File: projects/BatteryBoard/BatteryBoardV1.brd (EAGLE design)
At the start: 99 x 99 mm, 157 parts, among them M1 BSO201SP, U1 LTC4412MPS6, U2 SM74611, U3 LTC4121, U4 LTC4121, U5 LTC4121, U6 LTC4121

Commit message: Nearly finished placement of battery board, continued library updates and touch ups on all active boards/schematics.
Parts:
- removed U$4, U$6: BTS555, BrownSpaceEngineering:TO218-5
- removed U2: SM74611, BrownSpaceEngineering:TO-263
- added C23, C24, C26, C27: 10nF, BrownSpaceEngineering:0805
- added C25, C28: 150nF, BrownSpaceEngineering:0805
- added D7: DFLS130L, BrownSpaceEngineering:PWRDI-123
- added LIFE1TEMP, LIFE3TEMP, LION1TEMP, LION2TEMP: (no value), BrownSpaceEngineering:FLATPACK
- added R77, R80: 1K, BrownSpaceEngineering:0805
- added R78, R79, R81, R82: 4.7K, BrownSpaceEngineering:0805
- added R83: (no value), BrownSpaceEngineering:0805
- added SW1, SW2: BTS50015-1TAD, BrownSpaceEngineering:TO-263-7-8
- added V31: LIFEB1_OUTSNS, BrownSpaceEngineering:VIA-60MIL
- added V32: LION2SNS, BrownSpaceEngineering:VIA-60MIL
- added V33: LION2_RUN_CHG, BrownSpaceEngineering:VIA-60MIL
- added V34: LION1_RUN_DISG, BrownSpaceEngineering:VIA-60MIL
- added V35: LION2_RUN_DISG, BrownSpaceEngineering:VIA-60MIL
- added V36: LION1_STAT, BrownSpaceEngineering:VIA-60MIL
- added V37: LIONREF, BrownSpaceEngineering:VIA-60MIL
- added V38: LION2_STAT, BrownSpaceEngineering:VIA-60MIL
- added V39: UMB_CHG, BrownSpaceEngineering:VIA-60MIL-SQ
- added V40: LION1_RUN_CHG, BrownSpaceEngineering:VIA-60MIL-SQ
- added V41: LION1_FAULTN, BrownSpaceEngineering:VIA-60MIL-SQ
- added V42: LION1_CHGN, BrownSpaceEngineering:VIA-60MIL-SQ
- added V43: LION1SNS, BrownSpaceEngineering:VIA-60MIL-SQ
- added V44: LION1REF, BrownSpaceEngineering:VIA-60MIL-SQ
- added V45: LION1, BrownSpaceEngineering:VIA-60MIL-SQ
- added V46: LION1_RUN_DISG, BrownSpaceEngineering:VIA-60MIL-SQ
- added V47: LION1_STAT, BrownSpaceEngineering:VIA-60MIL-SQ
- added V48: LION_OUT, BrownSpaceEngineering:VIA-60MIL-SQ
- LI-ION1, LI-ION2, LIFEPO1, LIFEPO3: device BrownSpaceEngineering:EQUISAT-BATTERY -> BrownSpaceEngineering:EQUISAT-BATTERY-VA
- LIFEPO2, LIFEPO4: device BrownSpaceEngineering:EQUISAT-BATTERY -> BrownSpaceEngineering:EQUISAT-BATTERY-VB
- R31, R32: device BrownSpaceEngineering:0805 -> BrownSpaceEngineering:1210
- R41, R59: value 0.002R -> 0.002R@1W; device BrownSpaceEngineering:0805 -> BrownSpaceEngineering:1210
- R54, R72: value 34.8R@0.5W -> 34.8R@1W; device BrownSpaceEngineering:0805 -> BrownSpaceEngineering:1210
- R55, R73: value 34.8R@.5W -> 34.8R@1W; device BrownSpaceEngineering:0805 -> BrownSpaceEngineering:1210
- R58, R76: value 590R -> 1K
- V13: value LION1REF -> GND; device BrownSpaceEngineering:VIA-60MIL -> BrownSpaceEngineering:VIA-120MIL
- V21: device BrownSpaceEngineering:VIA-60MIL -> BrownSpaceEngineering:VIA-120MIL
- V22: value LIFEB2SNS -> GND; device BrownSpaceEngineering:VIA-60MIL -> BrownSpaceEngineering:VIA-120MIL
- V23: value LIFE_B2_RUNCHG -> SP_F_ST
- V24: value LIFE4 -> PANELREF
- V25: value LIFE3 -> LION1REF
- V26: value LIFE_B2_CHGN -> LION2_FAULTN
- V27: value LIFE_B2_FAULTN -> LION2_CHGN
- V28: value LIFE_B2_OUTEN -> LIFE_B2; device BrownSpaceEngineering:VIA-60MIL -> BrownSpaceEngineering:VIA-120MIL
- V29: value LIFE_B2 -> LION2REF
- V30: value LION_OU5 -> LION_OUT; device BrownSpaceEngineering:VIA-60MIL -> BrownSpaceEngineering:VIA-120MIL
- V7, V8: device BrownSpaceEngineering:VIA-60MIL -> BrownSpaceEngineering:VIA-60MIL-SQ
- moved V29 270.6 mm to (-6.00, -164.0)
- moved V27 251.2 mm to (-6.00, -141.0)
- moved V26 219.5 mm to (-6.00, -118.0)
- moved V25 214.3 mm to (-6.00, -95.0)
- moved V24 194.1 mm to (-6.00, -72.0)
- moved V23 145.4 mm to (-6.00, -49.0)
- moved R16 111.2 mm to (-2.00, 48.0)
- moved R31 109.9 mm to (27.6, 8.03), turned to 270 degrees
- moved C7 108.4 mm to (2.00, 47.0), flipped to the bottom, turned to 180 degrees
- moved R15 106.1 mm to (-2.00, 61.0), turned to 90 degrees
- moved R57 105.2 mm to (33.0, 40.0), turned to 90 degrees
- moved U$5 105.2 mm to (74.9, 39.0), turned to 0 degrees
- moved R32 104.6 mm to (6.64, 8.84), turned to 270 degrees
- moved C6 101.7 mm to (3.00, 62.0), flipped to the bottom, turned to 180 degrees
- moved R56 101.1 mm to (30.0, 40.0), turned to 90 degrees
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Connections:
- removed net N$34: U$4.P$2
- removed net N$44: U$6.P$2
- new net 5V: LIFE1TEMP.+, LIFE3TEMP.+, LION1TEMP.+, LION2TEMP.+
- new net LIFE1TEMP: LIFE1TEMP.-
- new net LIFE3TEMP: LIFE3TEMP.-
- new net LION1TEMP: LION1TEMP.-
- new net LION2TEMP: LION2TEMP.-
- new net N$1356: C28.2, R80.2, R81.2, SW2.P$2
- new net N$451: R76.2, R82.2, SW2.P$3
- new net N$68: C25.2, R77.2, R78.2, SW1.P$2
- new net N$686: R58.2, R79.2, SW1.P$3
- net 3V3: now also R83.2; no longer R37.2, R38.2
- net GND: now also C23.2, C24.2, C25.1, C26.2, C27.2, C28.1, R31.P$1, R32.P$1, R41.P$1, R59.P$1, R77.1, R80.1, SW1.P$1, SW2.P$1, V13.P$1, V22.P$1; no longer R31.1, R32.1, R41.1, R59.1
- net LIFE1: now also R54.P$2, SW1.PAD; no longer R54.2, U$4.P$3, U$4.PAD
- net LIFE2: now also R55.P$1; no longer R55.1
- net LIFE3: now also R72.P$2, SW2.PAD; no longer R72.2, U$6.P$3, U$6.PAD, V25.P$1
- net LIFE4: now also R73.P$1; no longer R73.1, V24.P$1
- net LIFEB1SNS: now also R41.P$2; no longer R41.2
- net LIFEB1_OUTSNS: now also C24.1, R79.1, V31.P$1; no longer R58.2, U$4.P$4
- net LIFEB2SNS: now also R59.P$2; no longer R59.2, V22.P$1
- net LIFEB2_OUTSNS: now also C27.1, R82.1; no longer R76.2, U$6.P$4
- net LIFE_B1: now also C23.1, SW1.P$5, SW1.P$6, SW1.P$7; no longer U$4.P$1, U$4.P$5
- net LIFE_B1_CHGN: now also U5.P$14
- net LIFE_B1_FAULTN: now also U5.P$15
- net LIFE_B1_OUTEN: now also R78.1
- net LIFE_B2: now also C26.1, SW2.P$5, SW2.P$6, SW2.P$7, V28.P$1; no longer U$6.P$1, U$6.P$5, V29.P$1
- net LIFE_B2_CHGN: now also U6.P$14; no longer V26.P$1
- net LIFE_B2_FAULTN: now also U6.P$15; no longer V27.P$1
- net LIFE_B2_OUTEN: now also R81.1; no longer V28.P$1
- net LIFE_B2_RUNCHG: no longer V23.P$1
- net LION1: now also V45.P$1
- net LION1REF: now also V25.P$1, V44.P$1; no longer V13.P$1
- net LION1SNS: now also R31.P$2, V43.P$1; no longer R31.2
- net LION1_CHGN: now also V42.P$1
- net LION1_FAULTN: now also V41.P$1
- net LION1_RUN_CHG: now also V40.P$1
- net LION1_RUN_DISG: now also V34.P$1, V46.P$1
- net LION1_STAT: now also V36.P$1, V47.P$1
- net LION2REF: now also V29.P$1
- net LION2SNS: now also R32.P$2, V32.P$1; no longer R32.2
- net LION2_CHGN: now also V27.P$1
- net LION2_FAULTN: now also V26.P$1
- net LION2_RUN_CHG: now also V33.P$1
- net LION2_RUN_DISG: now also V35.P$1
- net LION2_STAT: now also V38.P$1
- net LIONREF: now also V37.P$1
- net LION_OUT: now also R37.2, R38.2, V48.P$1
- net N$24: now also R54.P$1; no longer R54.1
- net N$25: now also R55.P$2; no longer R55.2
- net N$3: now also D7.A; no longer U2.P$1, U2.P$3
- net N$4: now also D7.C; no longer U2.PAD
- net N$42: now also R72.P$1; no longer R72.1
- net N$43: now also R73.P$2; no longer R73.2
- net PANELREF: now also V24.P$1
- net SP_F_ST: now also R83.1, V23.P$1
- net UMB_CHG: now also V39.P$1
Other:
- board size 99 x 99 mm -> 87 x 92 mm
- board text added: "Circular Vias are functional Square Vias are for debugging and test"

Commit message: Finished Battery Board layout and first draft of routing. Ready for final review. Additional library updates.
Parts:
- added C29, C30: 0.1uF, BrownSpaceEngineering:0805
- added R84: 1K, BrownSpaceEngineering:0805
- added R85, R86: 2.4K, BrownSpaceEngineering:0805
- added U$4: AD7991-0, BrownSpaceEngineering:SOT-23-8
- added U$6: TCA9535PWR, BrownSpaceEngineering:TSSOP-24
- added V49: SP_X_P, BrownSpaceEngineering:VIA-60MIL-SQ
- added V50: LIFE3TEMP, BrownSpaceEngineering:VIA-60MIL
- added V51: 3V3, BrownSpaceEngineering:VIA-60MIL
- added V52: SCL, BrownSpaceEngineering:VIA-60MIL
- added V53: SDA, BrownSpaceEngineering:VIA-60MIL
- added V54: LION_OUT, BrownSpaceEngineering:VIA-120MIL
- V11: value LION1_FAULTN -> !BATT_INT!
- V12: value LION1_CHGN -> GND; device BrownSpaceEngineering:VIA-60MIL -> BrownSpaceEngineering:VIA-60MIL-SQ
- V16, V17: device BrownSpaceEngineering:VIA-60MIL -> BrownSpaceEngineering:VIA-60MIL-SQ
- V23: value SP_F_ST -> GND; device BrownSpaceEngineering:VIA-60MIL -> BrownSpaceEngineering:VIA-120MIL
- V24: value PANELREF -> LION1TEMP
- V26: value LION2_FAULTN -> LIFE_B1; device BrownSpaceEngineering:VIA-60MIL -> BrownSpaceEngineering:VIA-120MIL
- V27: value LION2_CHGN -> LIFE_B2; device BrownSpaceEngineering:VIA-60MIL -> BrownSpaceEngineering:VIA-120MIL
- V32: value LION2SNS -> LION2TEMP
- V37: value LIONREF -> LIFE1TEMP
- V9: value LION1SNS -> 5V
- moved V48 631.6 mm to (22.0, 76.0)
- moved V47 608.5 mm to (19.0, 76.0)
- moved V46 585.4 mm to (15.0, 76.0)
- moved V45 559.3 mm to (13.0, 73.0)
- moved V44 535.2 mm to (7.00, 72.0), turned to 90 degrees
- moved V42 487.1 mm to (1.00, 70.0)
- moved V41 463.1 mm to (4.00, 69.0)
- moved V43 454.4 mm to (29.0, 13.0)
- moved V40 438.0 mm to (-2.00, 67.0)
- moved V39 435.7 mm to (19.0, 87.0)
- moved V38 401.5 mm to (29.0, 75.0)
- moved V36 358.9 mm to (19.0, 79.0)
- moved V35 329.9 mm to (29.0, 72.0), turned to 180 degrees
- moved V37 329.2 mm to (32.0, 25.0)
- moved V34 308.4 mm to (10.0, 75.0)
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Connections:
- new net !BATT_INT!: R84.1, U$6.P$1, V11.P$1
- new net SCL: R85.1, U$4.P$1, U$6.P$22, V52.P$1
- new net SDA: R86.1, U$4.P$2, U$6.P$23, V53.P$1
- net 3V3: now also C29.1, C30.1, R84.2, R85.2, R86.2, U$4.P$8, U$6.P$24, V51.P$1
- net 5V: now also V9.P$1
- net GND: now also C29.2, C30.2, U$4.P$7, U$6.P$12, U$6.P$2, U$6.P$21, U$6.P$3, U3.P$17, U3.P$5, V12.P$1, V23.P$1
- net LIFE1TEMP: now also V37.P$1
- net LIFE3TEMP: now also V50.P$1
- net LIFE_B1: now also V26.P$1
- net LIFE_B1_BOTT: now also U$6.P$13
- net LIFE_B1_CHGN: now also U$6.P$19
- net LIFE_B1_FAULTN: now also U$6.P$20
- net LIFE_B1_TOPT: now also U$6.P$14
- net LIFE_B2: now also V27.P$1
- net LIFE_B2_BOTT: now also U$6.P$16
- net LIFE_B2_CHGN: now also U$6.P$17
- net LIFE_B2_FAULTN: now also U$6.P$18
- net LIFE_B2_TOPT: now also U$6.P$15
- net LION1SNS: now also U$4.P$4; no longer V9.P$1
- net LION1TEMP: now also V24.P$1
- net LION1_CHGN: now also U$6.P$8; no longer V12.P$1
- net LION1_FAULTN: now also U$6.P$9; no longer V11.P$1
- net LION1_STAT: now also U$6.P$5
- net LION2SNS: now also U$4.P$3; no longer V32.P$1
- net LION2TEMP: now also V32.P$1
- net LION2_CHGN: now also U$6.P$10; no longer V27.P$1
- net LION2_FAULTN: now also U$6.P$11; no longer V26.P$1
- net LION2_STAT: now also U$6.P$4
- net LIONREF: now also U$4.P$5; no longer V37.P$1
- net LION_OUT: now also V54.P$1
- net PANELREF: now also U$4.P$6; no longer V24.P$1
- net SP_F_ST: now also U$6.P$6; no longer V23.P$1
- net SP_X_P: now also V49.P$1
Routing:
- net GND: track 0.00 -> 180.7 mm, vias 0 -> 46
- net 3V3: track 0.00 -> 178.1 mm, vias 0 -> 7
- net SP_OUT: track 0.00 -> 136.9 mm, vias 0 -> 3
- net LION2SNS: track 0.00 -> 82.2 mm, vias 0 -> 1
- net 5V: track 0.00 -> 81.5 mm, vias 0 -> 1
- net LIFE_B2_FAULTN: track 0.00 -> 65.3 mm, vias 0 -> 2
- net LION1SNS: track 0.00 -> 62.1 mm, vias 0 -> 1
- net LIFE_B1_CHGN: track 0.00 -> 60.5 mm, vias 0 -> 1
- net LIFE_B2_CHGN: track 0.00 -> 59.3 mm, vias 0 -> 2
- net LIFE1: track 0.00 -> 58.5 mm, vias 0 -> 1
- net LIFE3: track 0.00 -> 55.8 mm
- net LIFE4: track 0.00 -> 55.7 mm, vias 0 -> 1
- net LIFE_B2_BOTT: track 0.00 -> 54.0 mm
- net LIFE_B1_FAULTN: track 0.00 -> 54.0 mm
- net LION2: track 0.00 -> 53.4 mm, vias 0 -> 2
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- added copper zone on layer 1, net LIFE1
- added copper zone on layer 1, net LIFE3
- added copper zone on layer 1, net LIFE_B1
- added copper zone on layer 1, net LIFE_B2
- added copper zone on layer 1, net LION_OUT
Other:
- board text removed: "SP_FRNT"

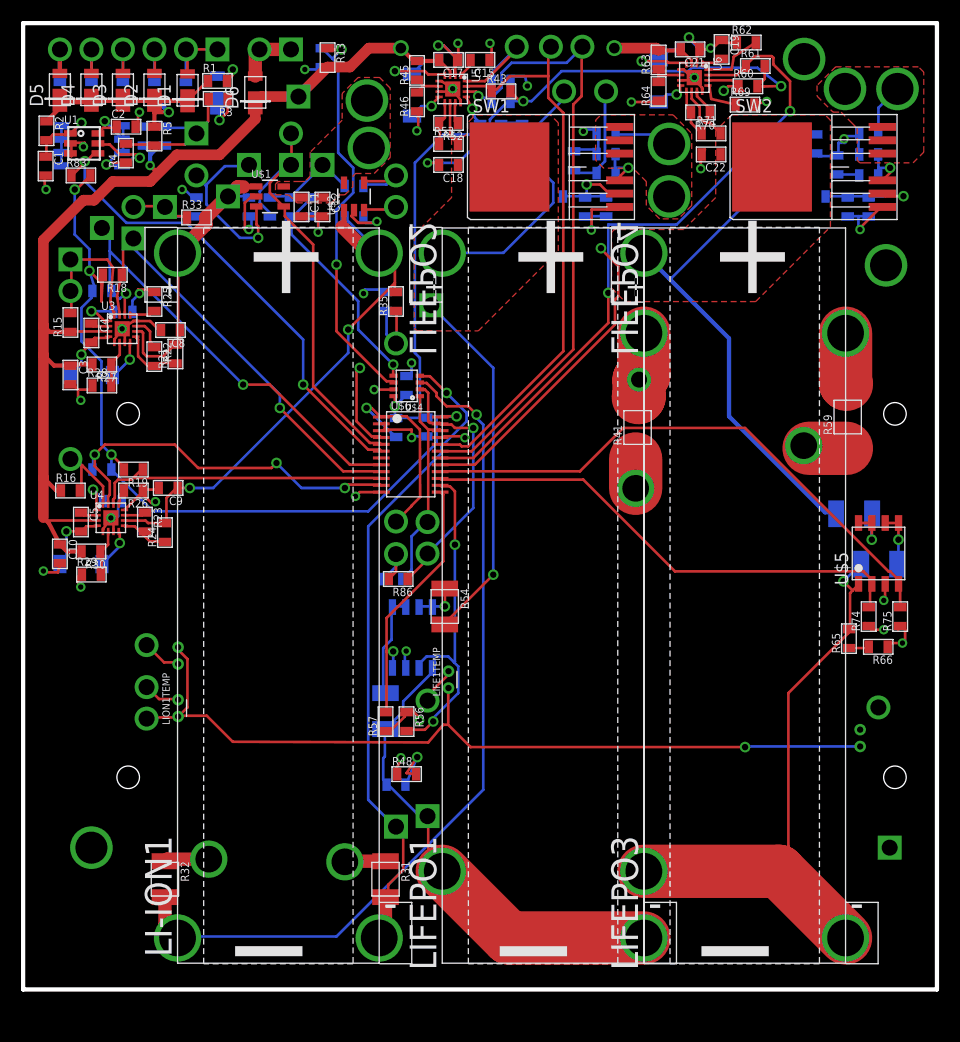
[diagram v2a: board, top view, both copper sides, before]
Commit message: Polishing up Battery Board layout
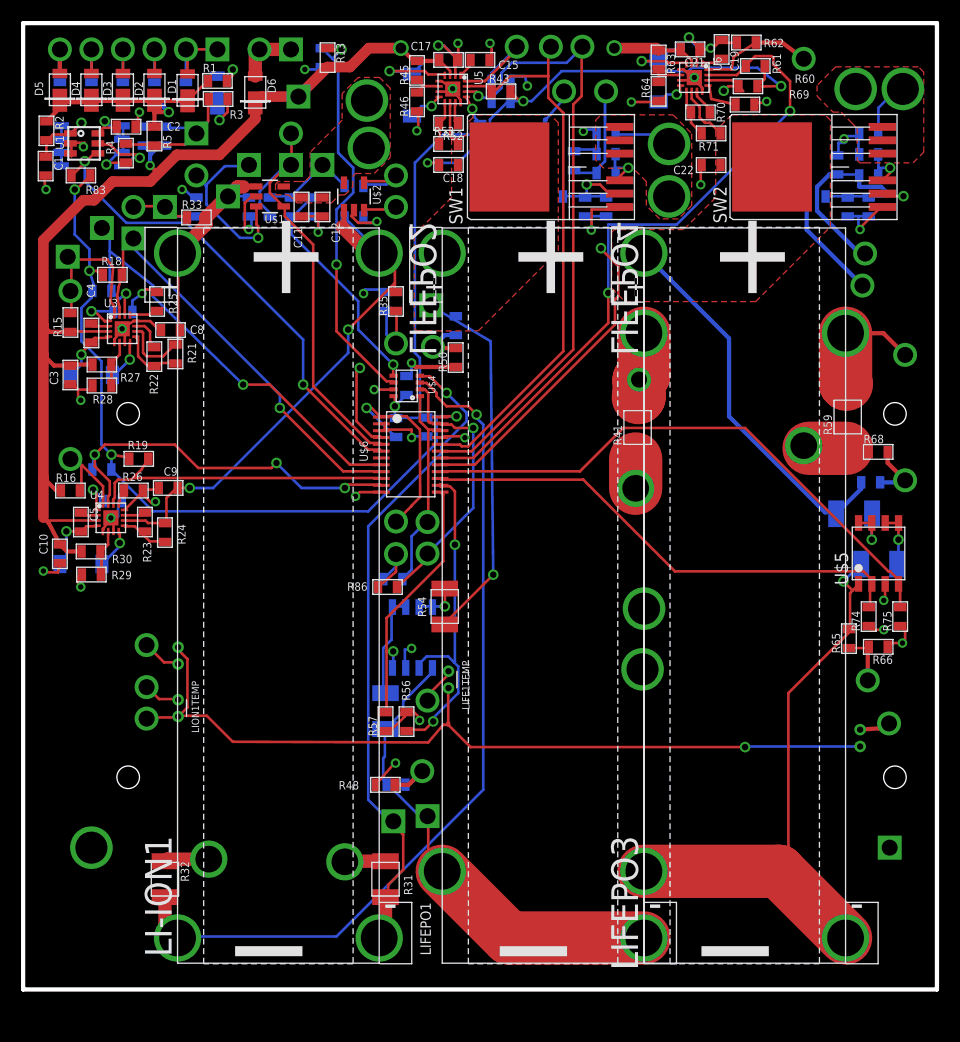
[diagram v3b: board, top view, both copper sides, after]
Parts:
- added V56: LF_B2_OUTEN, BrownSpaceEngineering:VIA-60MIL
- added V57: LF_B2_CHG, BrownSpaceEngineering:VIA-60MIL
- added V58: LF1_REF, BrownSpaceEngineering:VIA-60MIL
- added V59: LF2_REF, BrownSpaceEngineering:VIA-60MIL
- added V60: LF_B2_SNS, BrownSpaceEngineering:VIA-60MIL
- added V61: LF4_REF, BrownSpaceEngineering:VIA-60MIL
- added V62: LF3_REF, BrownSpaceEngineering:VIA-60MIL
- added V63: LF_B2_OSNS, BrownSpaceEngineering:VIA-60MIL
- LIFE1TEMP, LIFE3TEMP, LION1TEMP, LION2TEMP: value (none) -> AD590FLATPACK
- V10, V40: value LION1_RUN_CHG -> L1_CHG
- V15: value LIFE_B1_RUNCHG -> LF_B1_CHG
- V18: value LIFE_B1_CHGN -> LF_B1_CHGN
- V19: value LIFE_B1_FAULTN -> LF_B1_FAULTN
- V2, V49: value SP_X_P -> X_P
- V20: value LIFE_B1_OUTEN -> LF_B1_OUTEN
- V21, V26: value LIFE_B1 -> LF_B1
- V24: value LION1TEMP -> L1_TEMP
- V25, V44: value LION1REF -> L1_REF
- V29: value LION2REF -> L2_REF
- V3: value SP_X_N -> X_N
- V30, V48, V54: value LION_OUT -> L_OUT
- V31: value LIFEB1_OUTSNS -> LF_B1_OSNS
- V32: value LION2TEMP -> L2_TEMP
- V33: value LION2_RUN_CHG -> L2_CHG
- V34, V46: value LION1_RUN_DISG -> L1_DISG
- V35: value LION2_RUN_DISG -> L2_DISG
- V36, V47: value LION1_STAT -> L1_ST
- V37: value LIFE1TEMP -> LF1_TEMP
- V38: value LION2_STAT -> L2_ST
- V4: value SP_Z_P -> Z_P
- V41: value LION1_FAULTN -> L1_FAULTN
- V42: value LION1_CHGN -> L1_CHGN
- V43: value LION1SNS -> L1_SNS
- V5: value SP_Z_N -> Z_N
- V50: value LIFE3TEMP -> LF3_TEMP
- V6: value SP_Y_N -> Y_N
- moved V23 54.5 mm to (52.6, 33.8)
- moved V22 44.9 mm to (52.5, 28.0), turned to 270 degrees
- moved R67 33.0 mm to (74.2, 45.8), turned to 180 degrees
- moved R68 29.9 mm to (74.9, 48.7), flipped to the top, turned to 0 degrees
- moved R50 21.8 mm to (34.7, 57.7), flipped to the top
- moved R49 19.4 mm to (34.7, 60.7), turned to 270 degrees
- moved R48 2.27 mm to (28.0, 17.0)
- moved V50 1.83 mm to (75.9, 22.8)
- moved R86 1.27 mm to (28.2, 35.8)
- moved R19 1.14 mm to (4.51, 48.0)
- moved C22 1.02 mm to (59.0, 76.0)
- moved V27 1.02 mm to (72.8, 83.2)
- moved V43 0.57 mm to (28.7, 13.5)
- moved V28 0.51 mm to (77.3, 83.2)
- moved V40 0.36 mm to (-2.25, 67.3)
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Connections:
- net LIFE1TEMP renamed LF1_TEMP
- net LIFE3TEMP renamed LF3_TEMP
- net LIFEB1_OUTSNS renamed LF_B1_OSNS
- net LIFE_B1 renamed LF_B1
- net LIFE_B1_BOTT renamed LF_B1_BT
- net LIFE_B1_CHGN renamed LF_B1_CHGN
- net LIFE_B1_FAULTN renamed LF_B1_FAULTN
- net LIFE_B1_OUTEN renamed LF_B1_OUTEN
- net LIFE_B1_RUNCHG renamed LF_B1_CHG
- net LIFE_B1_TOPT renamed LF_B1_TT
- net LIFE_B2_BOTT renamed LF_B2_BT
- net LIFE_B2_CHGN renamed LF_B2_CHGN
- net LIFE_B2_FAULTN renamed LF_B2_FAULTN
- net LIFE_B2_TOPT renamed LF_B2_TT
- net LION1REF renamed L1_REF
- net LION1SNS renamed L1_SNS
- net LION1TEMP renamed L1_TEMP
- net LION1_CHGN renamed L1_CHGN
- net LION1_FAULTN renamed L1_FAULTN
- net LION1_RUN_CHG renamed L1_CHG
- net LION1_RUN_DISG renamed L1_DISG
- net LION1_STAT renamed L1_ST
- net LION2REF renamed L2_REF
- net LION2SNS renamed L2_SNS
- net LION2TEMP renamed L2_TEMP
- net LION2_CHGN renamed L2_CHGN
- net LION2_FAULTN renamed L2_FAULTN
- net LION2_RUN_CHG renamed L2_CHG
- net LION2_RUN_DISG renamed L2_DISG
- net LION2_STAT renamed L2_ST
- net LIONREF renamed L_REF
- net LION_OUT renamed L_OUT
- net SP_F_ST renamed SPF_ST
- net SP_X_N renamed X_N
- net SP_X_P renamed X_P
- net SP_Y_N renamed Y_N
- net SP_Z_N renamed Z_N
- net SP_Z_P renamed Z_P
- removed net LIFE1REF: R49.2, R50.2
- removed net LIFE2REF: R47.1, R48.2
- removed net LIFE3EF: R67.2, R68.2
- removed net LIFE4REF: R65.1, R66.2
- removed net LIFEB2SNS: LIFEPO4.MINUS, R59.P$2
- removed net LIFEB2_OUTSNS: C27.1, R82.1
- removed net LIFE_B2_OUTEN: R81.1
- removed net LIFE_B2_RUNCHG: R62.2, U6.P$16
- new net LF1_REF: R49.2, R50.2, V58.P$1
- new net LF2_REF: R47.1, R48.2, V59.P$1
- new net LF3_REF: R67.2, R68.2, V62.P$1
- new net LF4_REF: R65.1, R66.2, V61.P$1
- new net LF_B2_CHG: R62.2, U6.P$16, V57.P$1
- new net LF_B2_OSNS: C27.1, R82.1, V63.P$1
- new net LF_B2_OUTEN: R81.1, V56.P$1
- new net LF_B2_SNS: LIFEPO4.MINUS, R59.P$2, V60.P$1
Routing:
- net LIFE1: track 58.5 -> 40.2 mm
- net LF_B2_OSNS: track 0.00 -> 16.9 mm
- net LF_B2_SNS: track 0.00 -> 12.9 mm
- net LIFE3: track 55.8 -> 43.0 mm
- net LF_B2_CHG: track 0.00 -> 11.1 mm
- net LF_B2_OUTEN: track 0.00 -> 10.7 mm
- net LIFEB2SNS: track 6.35 -> 0.00 mm
- net LIFE_B2_RUNCHG: track 5.99 -> 0.00 mm
- net LF3_REF: track 0.00 -> 5.86 mm
- net LIFE2REF: track 5.60 -> 0.00 mm, vias 1 -> 0
- net LF2_REF: track 0.00 -> 5.28 mm
- net GND: track 180.7 -> 185.8 mm
- net LF4_REF: track 0.00 -> 5.08 mm
- net LF1_REF: track 0.00 -> 4.86 mm
- net 3V3: track 178.1 -> 174.7 mm
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
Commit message: Finished second round of Battery Board Layout
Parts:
- moved V13 19.2 mm to (-1.30, 30.2), turned to 90 degrees
- moved V12 3.72 mm to (74.5, 14.4)
- moved R10 1.78 mm to (-1.22, 83.0)
- moved R9 1.52 mm to (1.52, 83.0)
- moved V2 1.05 mm to (10.0, 86.7)
- moved R7 1.02 mm to (7.02, 83.0)
- moved R8 1.02 mm to (4.02, 83.0)
- moved V49 1.02 mm to (13.0, 87.0)
- moved R36 1.02 mm to (27.0, 63.0)
- moved V4 0.80 mm to (3.76, 86.7)
- moved V5 0.80 mm to (0.76, 86.7)
- moved V6 0.80 mm to (-2.24, 86.7)
- moved V3 0.80 mm to (6.76, 86.7)
- moved D3 0.76 mm to (3.76, 83.3)
- moved D4 0.76 mm to (0.76, 83.3)
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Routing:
- net SP_C: track 43.0 -> 47.9 mm
- net LION2: track 53.4 -> 56.9 mm
- net L2_REF: track 6.72 -> 5.55 mm
- net GND: track 185.8 -> 186.6 mm
- net UMB_CHG: track 5.71 -> 6.38 mm
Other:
- board size 87 x 92 mm -> 86.8 x 90.7 mm
- board text added: "BSE: EquiSat Battery Board V1 November 2016 Ryan Izant"
